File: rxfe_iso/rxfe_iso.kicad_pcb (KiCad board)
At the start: 2 copper layers, 24.9 x 51.3 mm, 14 parts, among them P1 CONN_02X08, P2 CONN_01X02, P3 CONN_02X08, U1 ADUM6400ARWZ, U2 ADUM7440

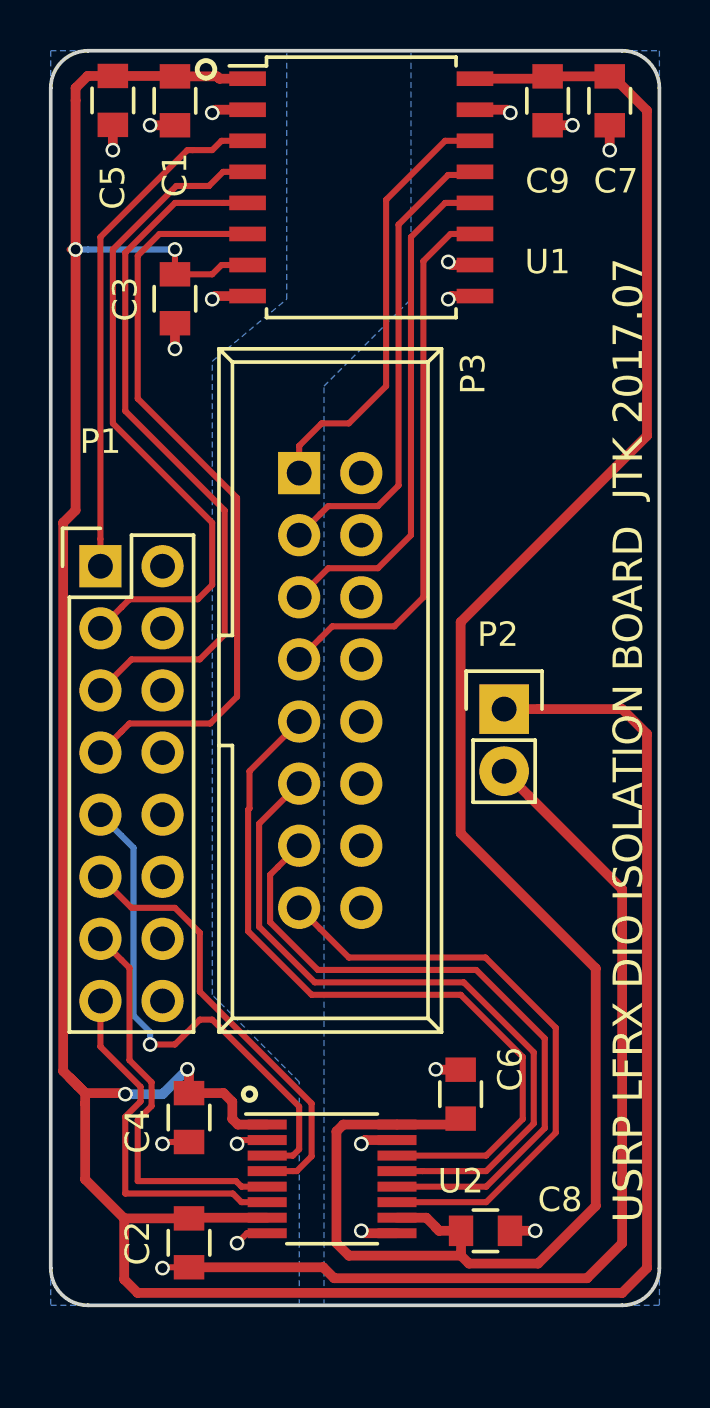
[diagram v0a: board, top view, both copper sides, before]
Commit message: moved headers on isolation boards to match actual measurements on lfrx and lftx usrp daughterboards, ready to order
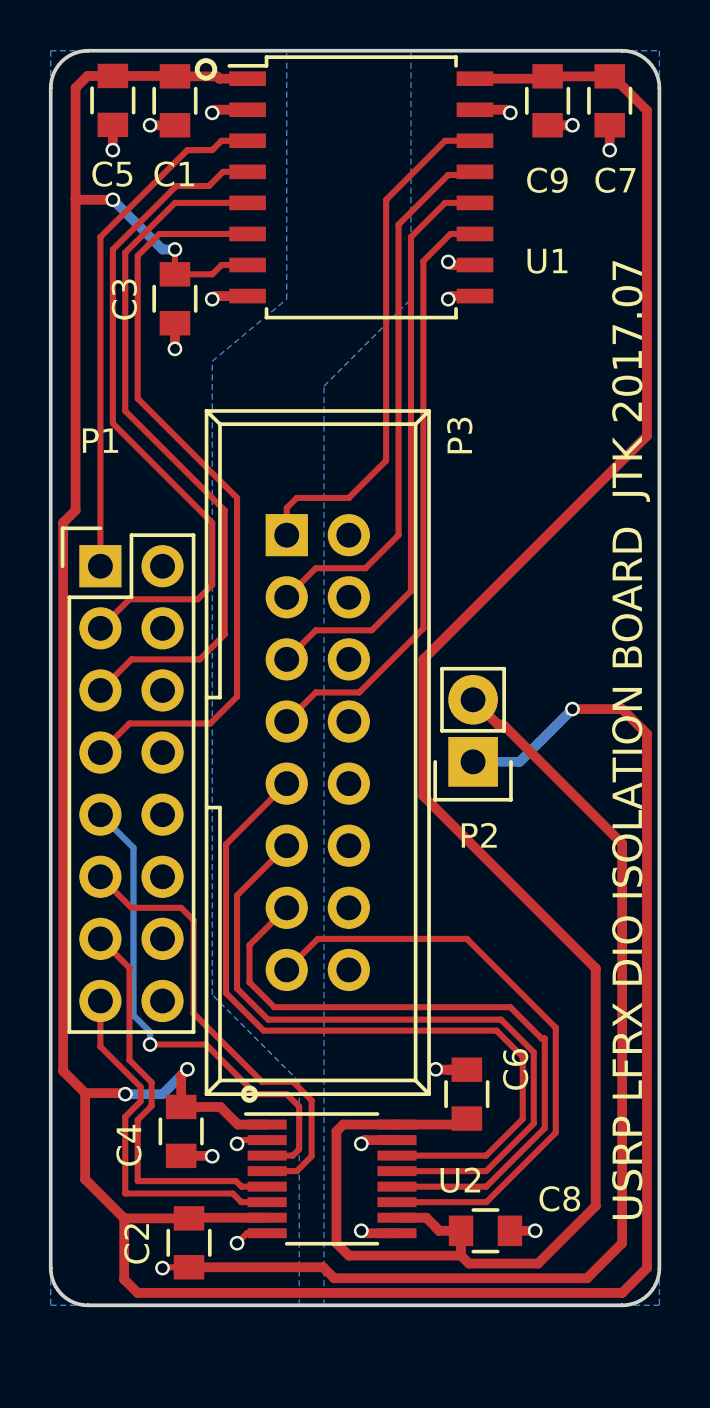
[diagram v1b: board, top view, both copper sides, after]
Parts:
- moved P3 2.59 mm to (231.1, 83.8)
- moved P2 2.50 mm to (238.8, 93.1), turned to 180 degrees
- moved C4 0.65 mm to (226.8, 108.2)
- moved C6 0.25 mm to (238.5, 106.7)
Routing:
- net GND: track 50.8 -> 54.5 mm
- net /ISO_DIO_1: track 17.9 -> 21.3 mm
- net /ISO_DIO_3: track 21.0 -> 23.9 mm
- net /ISO_DIO_2: track 19.6 -> 22.3 mm
- net /ISO_DIO_4: track 22.5 -> 24.8 mm
- net +3V3: track 132.4 -> 134.5 mm, vias 4 -> 5
- net VDD: track 84.3 -> 85.8 mm
- net /ISO_IN_6: track 18.1 -> 19.0 mm
- net /ISO_IN_5: track 21.4 -> 20.5 mm
- net GNDA: track 10.9 -> 11.7 mm
- net /ISO_DIO_8: track 24.5 -> 25.0 mm
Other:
- rule pad_to_mask_clearance: 0.2 -> 0.1

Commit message: dfm changes to isolation boards, increased annual ring size and copper to edge clearance. ordered boards
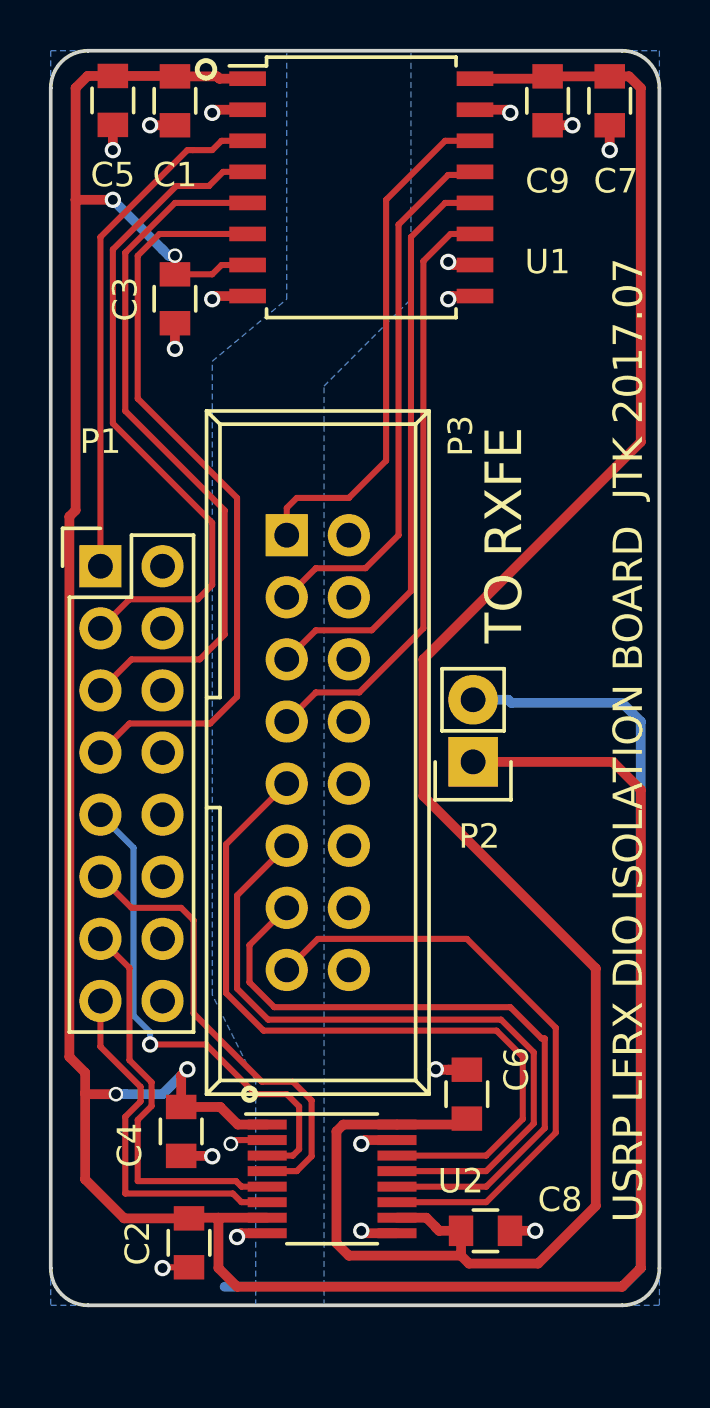
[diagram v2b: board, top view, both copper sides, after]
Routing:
- net +3V3: track 134.5 -> 126.2 mm, vias 5 -> 4
- net GND: track 54.5 -> 58.2 mm
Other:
- net class Default: clearance 0.2 -> 0.19812
- rule trace_clearance: 0.2 -> 0.19812
- rule trace_min: 0.2 -> 0.20066
- board text added: "TO RXFE"

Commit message: added rf-front end module for mcmurdo USRP upgrade
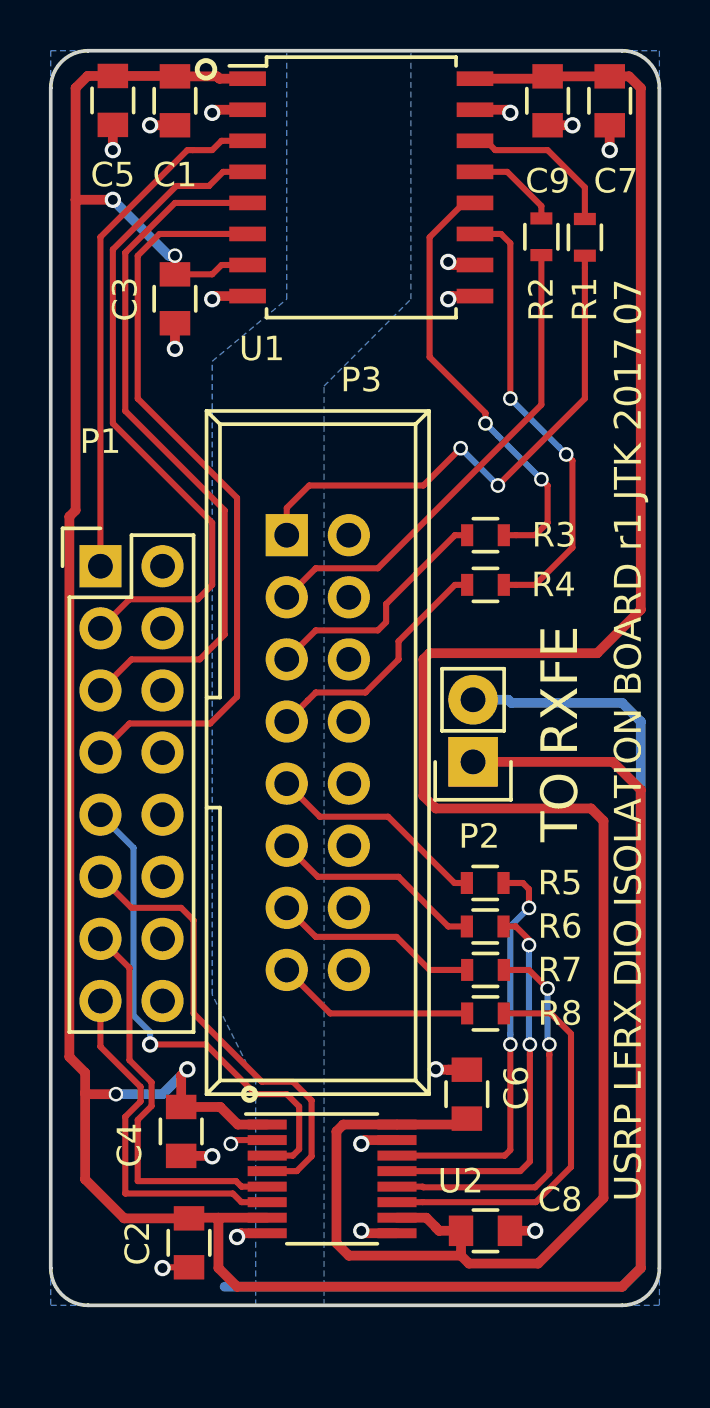
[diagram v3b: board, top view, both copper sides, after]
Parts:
- added R1: 2k2, Resistors_SMD:R_0603, F.Cu at (243.3, 71.6)
- added R2: 2k2, Resistors_SMD:R_0603, F.Cu at (241.6, 71.6)
- added R3: 2k2, Resistors_SMD:R_0603, F.Cu at (239.3, 83.8)
- added R4: 2k2, Resistors_SMD:R_0603, F.Cu at (239.3, 85.9)
- added R5: 2k2, Resistors_SMD:R_0603, F.Cu at (239.3, 98.0)
- added R6: 2k2, Resistors_SMD:R_0603, F.Cu at (239.3, 99.8)
- added R7: 2k2, Resistors_SMD:R_0603, F.Cu at (239.3, 101.6)
- added R8: 2k2, Resistors_SMD:R_0603, F.Cu at (239.3, 103.4)
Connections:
- P3 pad 1: /ISO_DIO_1 -> Net-(P3-Pad1)
- P3 pad 11: /ISO_DIO_6 -> Net-(P3-Pad11)
- P3 pad 13: /ISO_DIO_7 -> Net-(P3-Pad13)
- P3 pad 15: /ISO_DIO_8 -> Net-(P3-Pad15)
- P3 pad 3: /ISO_DIO_2 -> Net-(P3-Pad3)
- P3 pad 5: /ISO_DIO_3 -> Net-(P3-Pad5)
- P3 pad 7: /ISO_DIO_4 -> Net-(P3-Pad7)
- P3 pad 9: /ISO_DIO_5 -> Net-(P3-Pad9)
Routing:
- net Net-(P3-Pad1): track 0.00 -> 22.3 mm, vias 0 -> 2
- net Net-(P3-Pad3): track 0.00 -> 19.8 mm
- net /ISO_DIO_2: track 22.3 -> 4.43 mm
- net /ISO_DIO_1: track 21.3 -> 6.58 mm
- net /ISO_DIO_5: track 31.1 -> 16.9 mm, vias 0 -> 2
- net /ISO_DIO_6: track 29.2 -> 15.9 mm, vias 0 -> 2
- net /ISO_DIO_7: track 27.4 -> 16.2 mm, vias 0 -> 2
- net Net-(P3-Pad7): track 0.00 -> 10.1 mm
- net Net-(P3-Pad5): track 0.00 -> 9.92 mm
- net Net-(P3-Pad9): track 0.00 -> 9.05 mm
- net /ISO_DIO_8: track 25.0 -> 16.3 mm
- net Net-(P3-Pad11): track 0.00 -> 8.73 mm
- net Net-(P3-Pad13): track 0.00 -> 8.43 mm
- net Net-(P3-Pad15): track 0.00 -> 8.11 mm
- net VDD: track 86.1 -> 94.1 mm
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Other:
- board text added: "USRP LFRX DIO ISOLATION BOARD r1 JTK 2017.07"
- board text removed: "USRP LFRX DIO ISOLATION BOARD JTK 2017.07"
